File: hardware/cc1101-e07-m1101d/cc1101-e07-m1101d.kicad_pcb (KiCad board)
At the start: 2 copper layers, 15 x 30 mm, 4 parts, among them J1 Conn_02x04_Odd_Even, J2 Conn_Coaxial

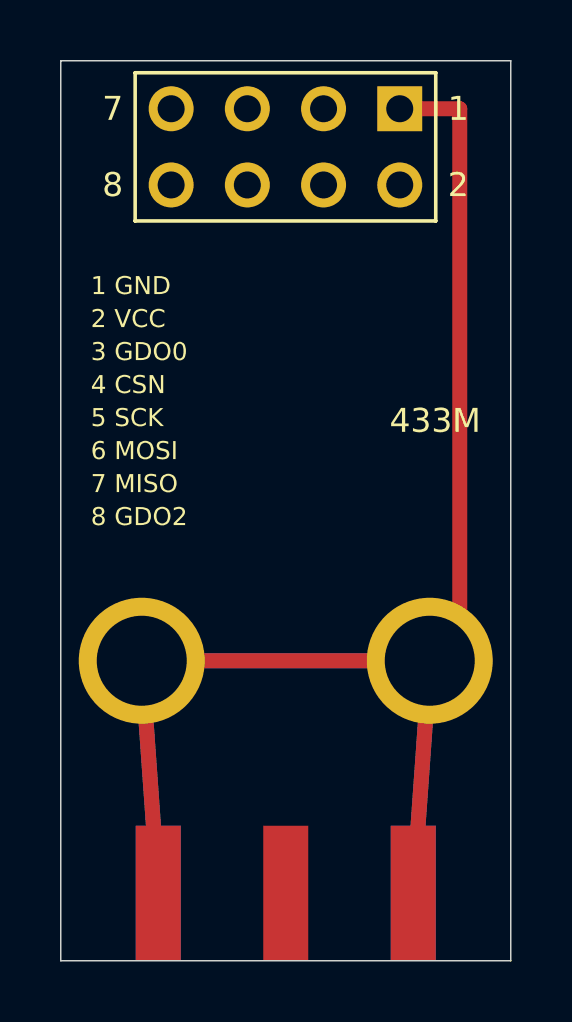
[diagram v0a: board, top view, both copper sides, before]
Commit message: Merge the two socket adapters into esp32c3-radio-adapter; two-sided pin silk on the replicas
* esp32c3-radio-adapter replaces esp32c3-cc1101-adapter and
  esp32c3-ra02-adapter: the E07-M1101D and Ra-02 breakout headers differ
  only at outer column 3 (GDO0 / RST) and inner column 1 (GDO2 / DIO0),
  wired to GPIO10 and GPIO3, so one socket takes either board.  Nets are
  named GDO0_RST, GDO2_DIO0 and CSN_NSS; the silk carries the E07 names
  with the Ra-02 names in parentheses, plus both boards' fab outlines.
* Ra-02 breakout replica: header and module pin numbers on the back silk;
  header pin names beside each column on both sides.
* E07-M1101D replica: pin names beside each column on both sides; the
  markers, box and legend are mirrored onto the back.
* Pinout diagrams combined into docs/images/pinout-radio-boards.svg.
* README, export defaults and generator lists updated.

Co-Authored-By: Claude Fable 5.1 <noreply@anthropic.com>
Claude-Session: https://claude.ai/code/session_01JoGdh4Cg3VtTTDZi4gQuiN
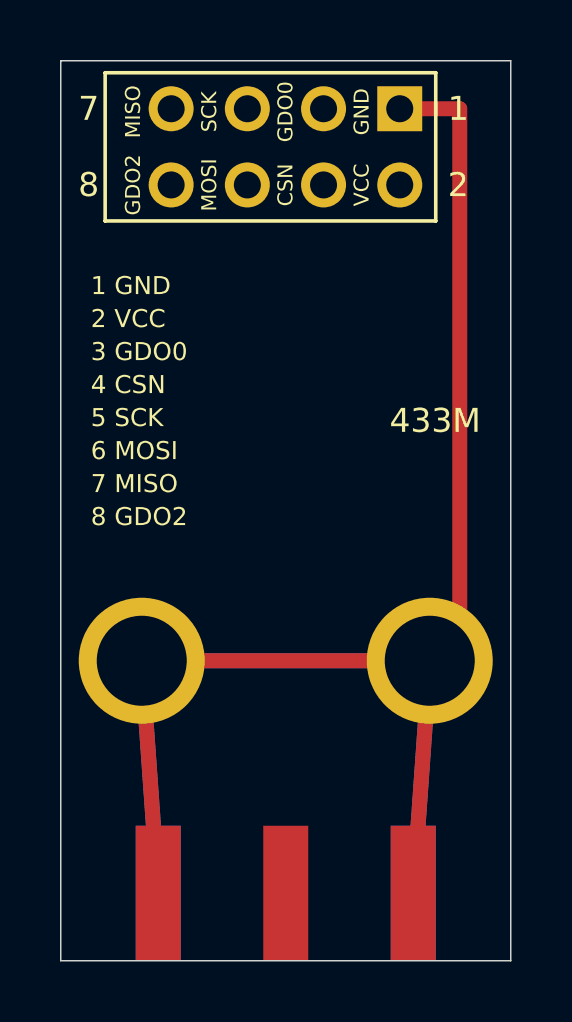
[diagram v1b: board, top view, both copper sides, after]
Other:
- board text added: "CSN"
- board text added: "GDO0"
- board text added: "GDO2"
- board text added: "GND"
- board text added: "MISO"
- board text added: "MOSI"
- board text added: "SCK"
- board text added: "VCC"
